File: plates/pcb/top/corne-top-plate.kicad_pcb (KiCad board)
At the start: 2 copper layers, 132.9 x 91.4 mm, 26 parts, among them SW2 KEY_SWITCH

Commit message: Update pcb plates
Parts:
- added G***: LOGO, kbd:corne-logo-horizontal-mask, B.Cu at (108.1, 122.0)
- added G***: LOGO, kbd:corne-logo-horizontal-mask, F.Cu at (108.3, 121.9)
- ? (x5): footprint kbd:M2_HOLE_v3 -> kbd:M2_Hole_TH
- SW2 (x21): footprint kbd:SW_Hole_TH -> kbd:SW_Hole
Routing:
- added copper zone on B.Cu, net (none)
- added copper zone on F.Cu, net (none)
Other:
- outline, holes or cut-outs redrawn
- board text removed: "Corne Keyboard PCB Designed by foostan"

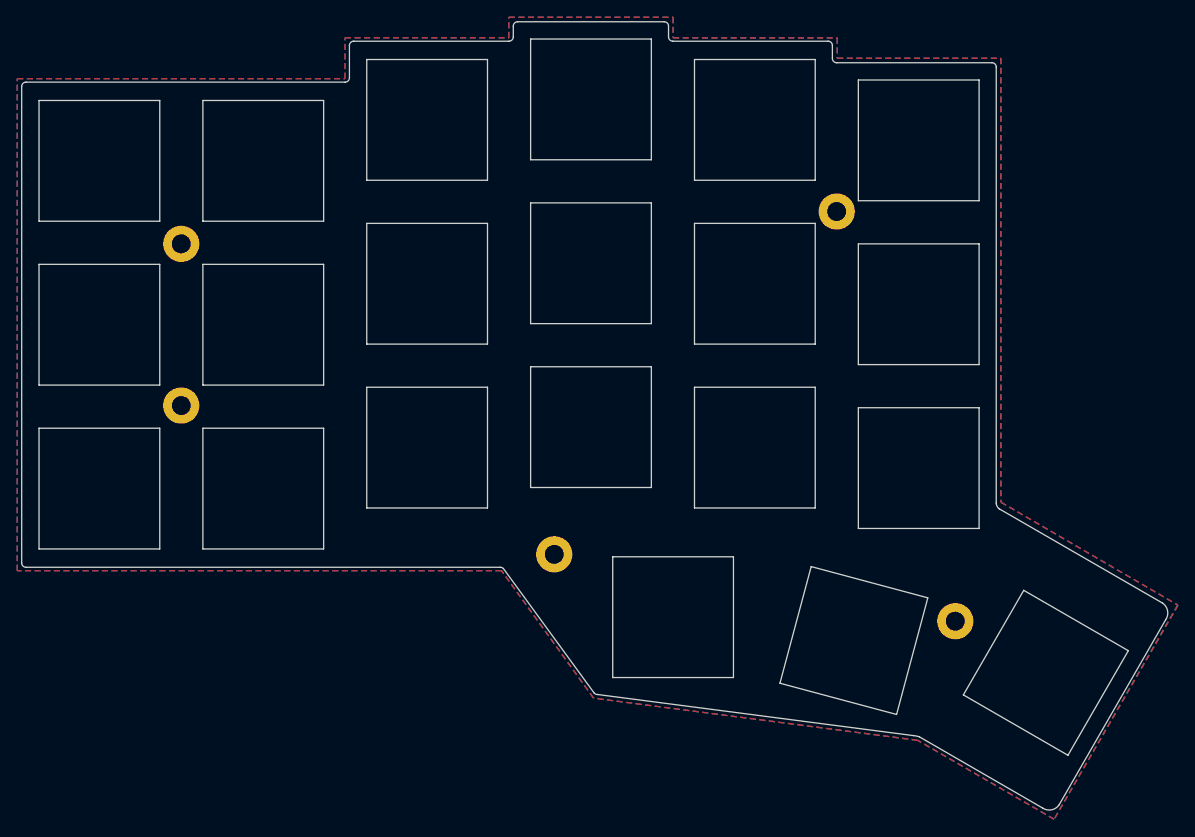
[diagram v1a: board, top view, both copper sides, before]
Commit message: Fix hole size
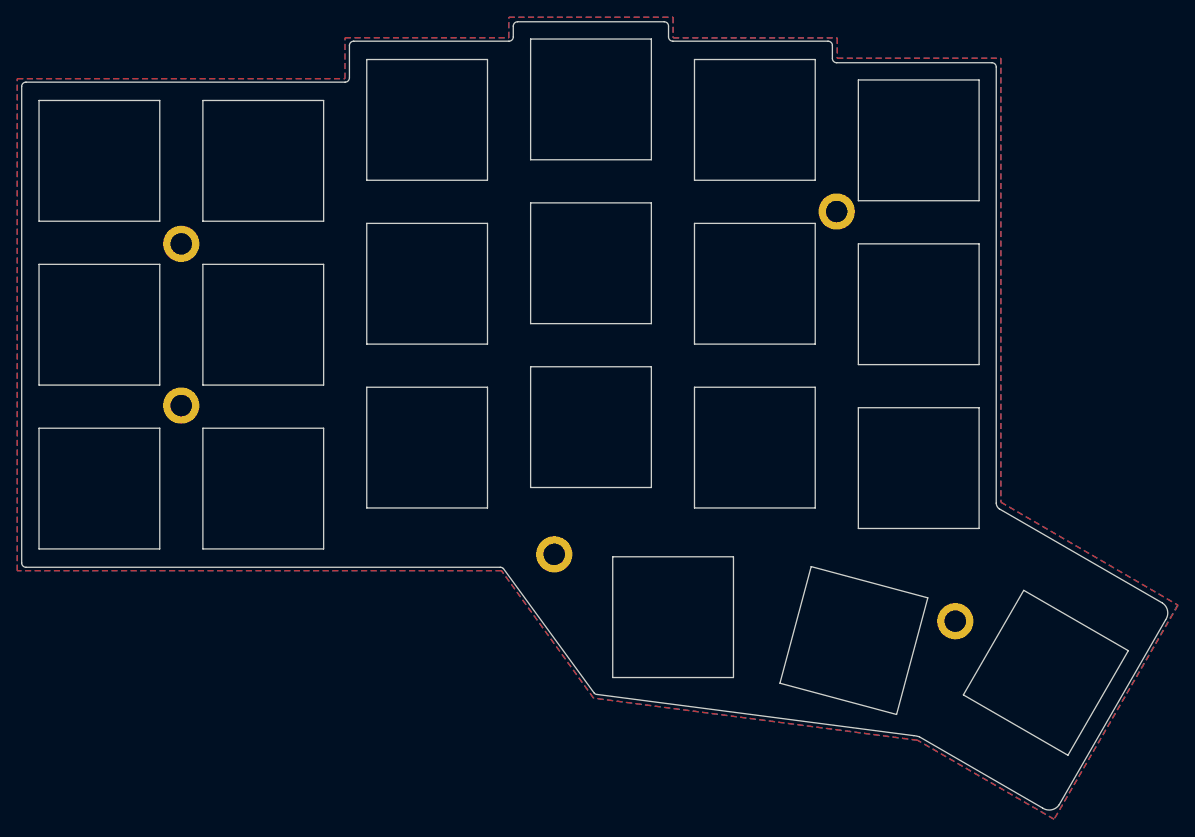
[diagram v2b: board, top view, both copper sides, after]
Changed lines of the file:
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@@
       (effects (font (size 1 1) (thickness 0.15)))
     )
-    (pad "" thru_hole circle (at 0 0) (size 4.2 4.2) (drill 2.2) (layers *.Cu *.Mask))
+    (pad "" thru_hole circle (at 0 0) (size 4.2 4.2) (drill 2.5) (layers *.Cu *.Mask))
   )
   (module kbd:M2_Hole_TH (layer F.Cu)
@@
       (effects (font (size 1 1) (thickness 0.15)))
     )
-    (pad "" thru_hole circle (at 0 0) (size 4.2 4.2) (drill 2.2) (layers *.Cu *.Mask))
+    (pad "" thru_hole circle (at 0 0) (size 4.2 4.2) (drill 2.5) (layers *.Cu *.Mask))
   )
   (module kbd:M2_Hole_TH (layer F.Cu)
@@
       (effects (font (size 1 1) (thickness 0.15)))
     )
-    (pad "" thru_hole circle (at 0 0) (size 4.2 4.2) (drill 2.2) (layers *.Cu *.Mask))
+    (pad "" thru_hole circle (at 0 0) (size 4.2 4.2) (drill 2.5) (layers *.Cu *.Mask))
   )
   (module kbd:M2_Hole_TH (layer F.Cu)
@@
       (effects (font (size 1 1) (thickness 0.15)))
     )
-    (pad "" thru_hole circle (at 0 0) (size 4.2 4.2) (drill 2.2) (layers *.Cu *.Mask))
+    (pad "" thru_hole circle (at 0 0) (size 4.2 4.2) (drill 2.5) (layers *.Cu *.Mask))
   )
   (module kbd:M2_Hole_TH (layer F.Cu)
@@
       (effects (font (size 1 1) (thickness 0.15)))
     )
-    (pad "" thru_hole circle (at 0 0) (size 4.2 4.2) (drill 2.2) (layers *.Cu *.Mask))
+    (pad "" thru_hole circle (at 0 0) (size 4.2 4.2) (drill 2.5) (layers *.Cu *.Mask))
   )
   (module kbd:corne-logo-horizontal-mask (layer B.Cu)

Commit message: Fix hole size
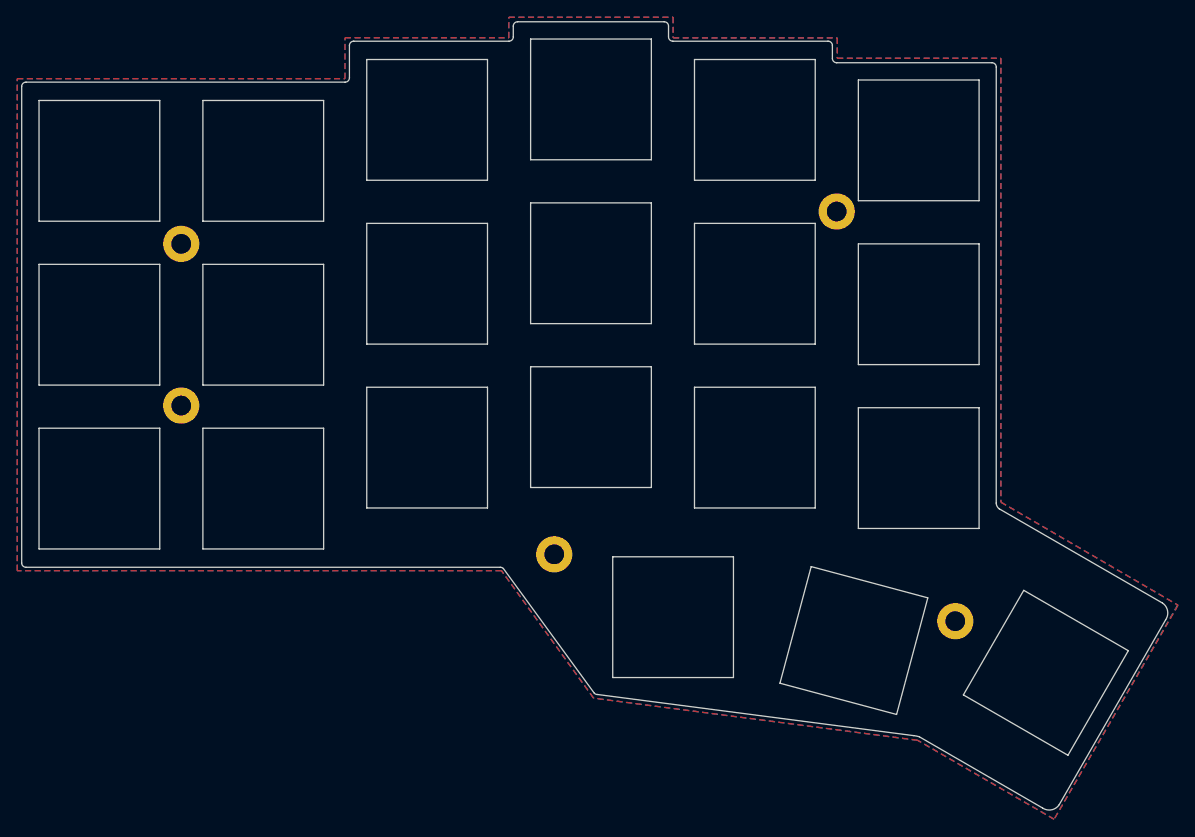
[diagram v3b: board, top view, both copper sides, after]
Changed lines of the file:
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@@
       (effects (font (size 1 1) (thickness 0.15)))
     )
-    (pad "" thru_hole circle (at 0 0) (size 4.2 4.2) (drill 2.5) (layers *.Cu *.Mask))
+    (pad "" thru_hole circle (at 0 0) (size 4.2 4.2) (drill 2.3) (layers *.Cu *.Mask))
   )
   (module kbd:M2_Hole_TH (layer F.Cu)
@@
       (effects (font (size 1 1) (thickness 0.15)))
     )
-    (pad "" thru_hole circle (at 0 0) (size 4.2 4.2) (drill 2.5) (layers *.Cu *.Mask))
+    (pad "" thru_hole circle (at 0 0) (size 4.2 4.2) (drill 2.3) (layers *.Cu *.Mask))
   )
   (module kbd:M2_Hole_TH (layer F.Cu)
@@
       (effects (font (size 1 1) (thickness 0.15)))
     )
-    (pad "" thru_hole circle (at 0 0) (size 4.2 4.2) (drill 2.5) (layers *.Cu *.Mask))
+    (pad "" thru_hole circle (at 0 0) (size 4.2 4.2) (drill 2.3) (layers *.Cu *.Mask))
   )
   (module kbd:M2_Hole_TH (layer F.Cu)
@@
       (effects (font (size 1 1) (thickness 0.15)))
     )
-    (pad "" thru_hole circle (at 0 0) (size 4.2 4.2) (drill 2.5) (layers *.Cu *.Mask))
+    (pad "" thru_hole circle (at 0 0) (size 4.2 4.2) (drill 2.3) (layers *.Cu *.Mask))
   )
   (module kbd:M2_Hole_TH (layer F.Cu)
@@
       (effects (font (size 1 1) (thickness 0.15)))
     )
-    (pad "" thru_hole circle (at 0 0) (size 4.2 4.2) (drill 2.5) (layers *.Cu *.Mask))
+    (pad "" thru_hole circle (at 0 0) (size 4.2 4.2) (drill 2.3) (layers *.Cu *.Mask))
   )
   (module kbd:corne-logo-horizontal-mask (layer B.Cu)

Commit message: plates
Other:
- net class Default removed
